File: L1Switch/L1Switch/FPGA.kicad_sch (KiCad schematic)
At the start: 9 parts, among them J11 Conn_01x06_Male, U1 XC7A35T-FTG256, X1 LFSPXO076034CUTT

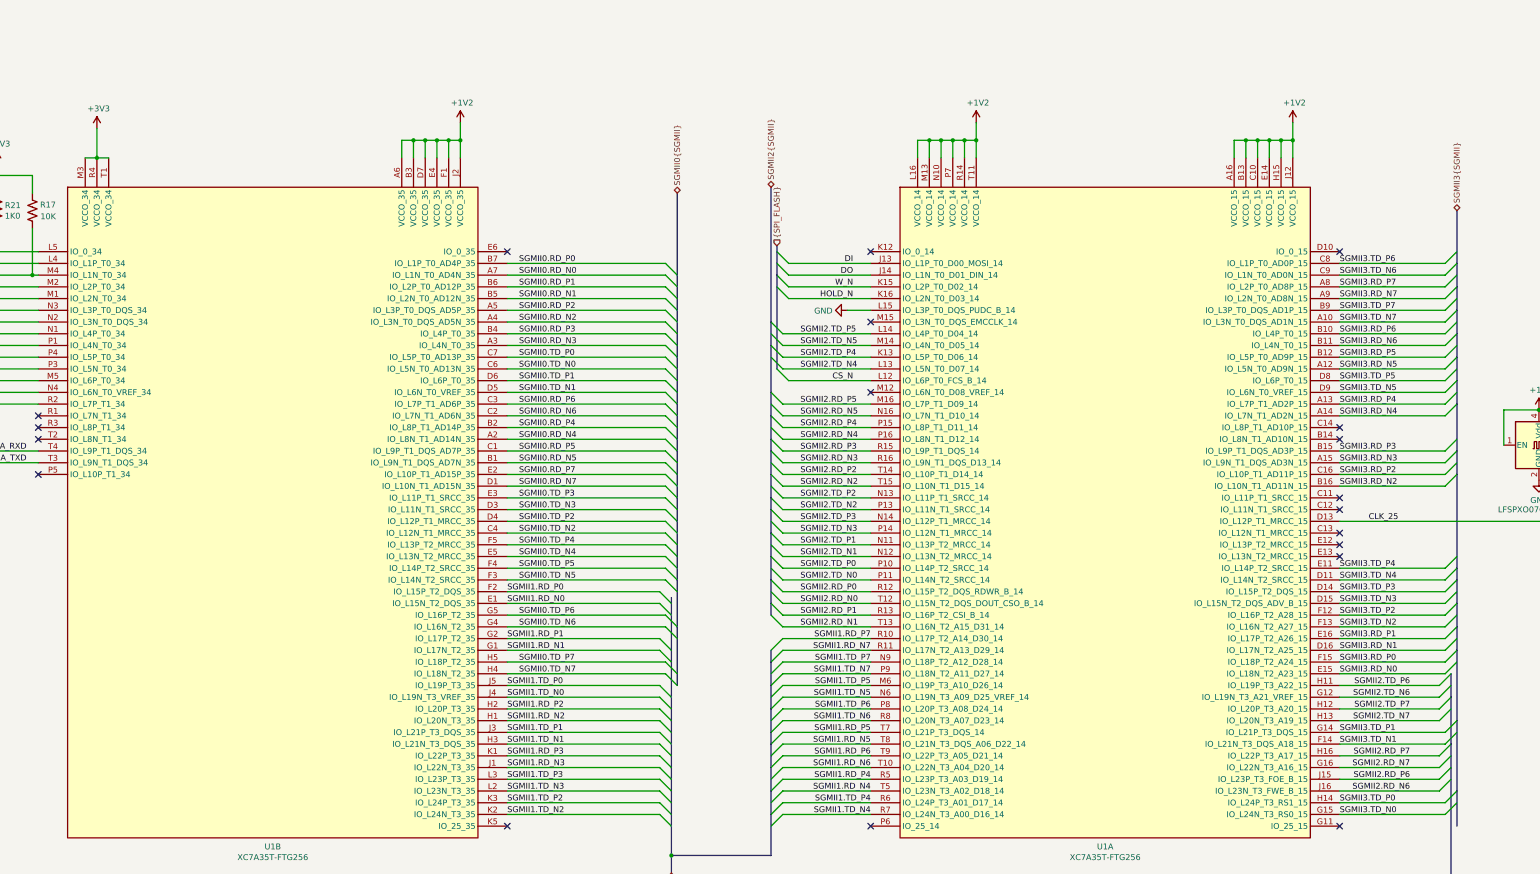
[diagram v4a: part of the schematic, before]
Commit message: Add FPGA decoupling caps. Add some power planes.
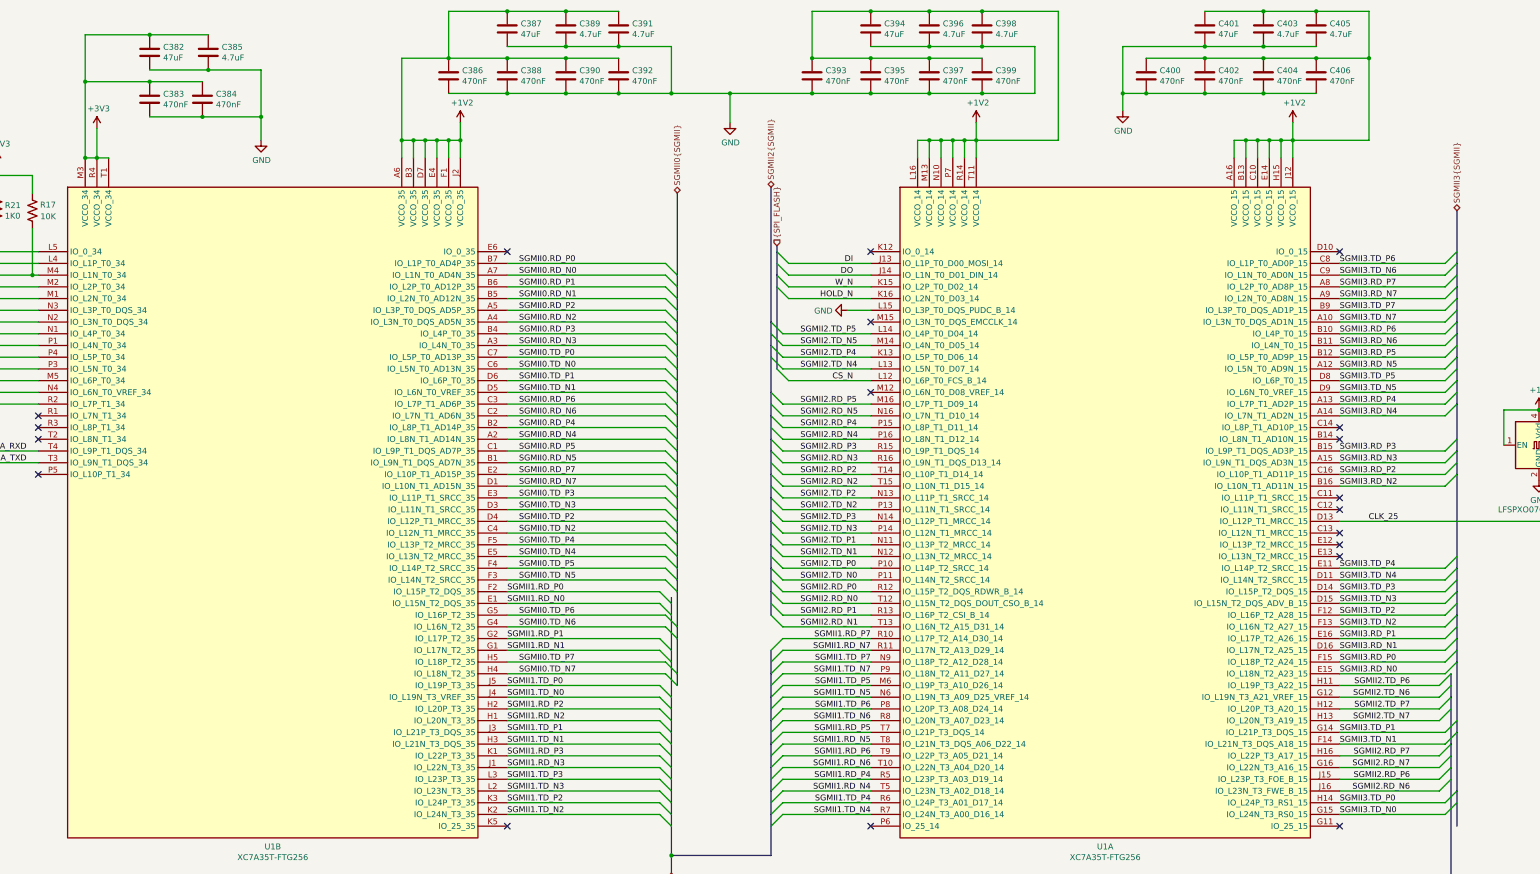
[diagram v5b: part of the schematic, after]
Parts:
- added C382, C387, C394, C401: 47uF, Capacitor_SMD:C_1210_3225Metric, symbol Device:C
- added C383, C384, C386, C388, C390, C392, C393, C395, C397, C399, C400, C402, C404, C406: 470nF, Capacitor_SMD:C_0402_1005Metric, symbol Device:C
- added C385, C389, C391, C396, C398, C403, C405: 4.7uF, Capacitor_SMD:C_0805_2012Metric, symbol Device:C
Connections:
- net +1V2: now also C386.1, C387.1, C388.1, C389.1, C390.1, C391.1, C392.1, C393.1, C394.1, C395.1, C396.1, C397.1, C398.1, C399.1, C400.1, C401.1, C402.1, C403.1, C404.1, C405.1, C406.1
- net +3V3: now also C382.1, C383.1, C384.1, C385.1
- net GND: now also C382.2, C383.2, C384.2, C385.2, C386.2, C387.2, C388.2, C389.2, C390.2, C391.2, C392.2, C393.2, C394.2, C395.2, C396.2, C397.2, C398.2, C399.2, C400.2, C401.2, C402.2, C403.2, C404.2, C405.2, C406.2

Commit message: Add some part info. Fix footprint size for 2kV caps. Add a plane cutout around the magnetics.
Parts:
- C382, C387, C394, C401: value 47uF -> 47 uF; MFR Part# (none) -> GRM32EB31A476KE20L; Manufacturer (none) -> MuRata
- C383, C384, C386, C388, C390, C392, C393, C395, C397, C399, C400, C402, C404, C406: value 470nF -> 470 nF; MFR Part# (none) -> GRM155R61C474KE01D; Manufacturer (none) -> MuRata
- C385, C389, C391, C396, C398, C403, C405: value 4.7uF -> 4.7 uF; MFR Part# (none) -> C0805C475K9PAC; Manufacturer (none) -> Kemet
- J11: MFR Part# (none) -> 68000-106HLF; Manufacturer (none) -> Amphenol
- U1: MFR Part# (none) -> XC7A35T-2FTG256C; Manufacturer (none) -> Xilinx
- X1: MFR Part# (none) -> LFSPXO076034CUTT; Manufacturer (none) -> IQD

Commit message: Update part numbers.
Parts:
- R135, R136, R137, R21: MFR Part# (none) -> CRCW04021K00FKEE; Manufacturer (none) -> Vishay
- R17: value 10K -> 10K0; MFR Part# (none) -> CRCW040210K0FKED; Manufacturer (none) -> Vishay
- TP1: MFR Part# (none) -> -; Manufacturer (none) -> -
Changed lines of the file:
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@@
 (kicad_sch (version 20200608) (host eeschema "5.99.0-unknown-1973153~101~ubuntu20.04.1")
-  (page 2 12)
+  (page 1 12)
   (paper "B")
   (bus_alias "MAC1_SGMII" (members ))
@@
   (junction (at 414.02 125.73))
   (junction (at 213.36 198.12))
+  (no_connect (at 358.14 107.95))
+  (no_connect (at 256.54 82.55))
   (no_connect (at 76.2 105.41))
-  (no_connect (at 358.14 105.41))
+  (no_connect (at 46.99 116.84))
+  (no_connect (at 177.8 67.31))
+  (no_connect (at 76.2 107.95))
+  (no_connect (at 358.14 120.65))
+  (no_connect (at 76.2 115.57))
+  (no_connect (at 358.14 133.35))
+  (no_connect (at 358.14 191.77))
+  (no_connect (at 256.54 67.31))
+  (no_connect (at 358.14 128.27))
+  (no_connect (at 358.14 130.81))
+  (no_connect (at 256.54 191.77))
+  (no_connect (at 46.99 114.3))
+  (no_connect (at 177.8 191.77))
   (no_connect (at 46.99 124.46))
-  (no_connect (at 177.8 191.77))
-  (no_connect (at 177.8 67.31))
-  (no_connect (at 76.2 102.87))
-  (no_connect (at 358.14 120.65))
-  (no_connect (at 358.14 128.27))
-  (no_connect (at 358.14 191.77))
-  (no_connect (at 358.14 130.81))
-  (no_connect (at 358.14 133.35))
-  (no_connect (at 76.2 107.95))
-  (no_connect (at 256.54 67.31))
-  (no_connect (at 256.54 191.77))
-  (no_connect (at 76.2 115.57))
-  (no_connect (at 256.54 82.55))
-  (no_connect (at 46.99 116.84))
   (no_connect (at 256.54 97.79))
   (no_connect (at 358.14 123.19))
   (no_connect (at 358.14 67.31))
-  (no_connect (at 358.14 107.95))
-  (no_connect (at 46.99 114.3))
+  (no_connect (at 358.14 105.41))
+  (no_connect (at 76.2 102.87))
   (bus_entry (at 210.82 140.97) (size 2.54 2.54))
   (bus_entry (at 210.82 143.51) (size 2.54 2.54))
@@
     (stroke (width 0) (type solid) (color 0 0 0 0))
   )
-  (bus (pts (xy 214.63 54.61) (xy 214.63 72.39))
-    (stroke (width 0) (type solid) (color 0 0 0 0))
-  )
-  (bus (pts (xy 214.63 72.39) (xy 214.63 77.47))
-    (stroke (width 0) (type solid) (color 0 0 0 0))
-  )
-  (bus (pts (xy 214.63 77.47) (xy 214.63 80.01))
-    (stroke (width 0) (type solid) (color 0 0 0 0))
-  )
-  (bus (pts (xy 214.63 80.01) (xy 214.63 85.09))
+  (bus (pts (xy 214.63 54.61) (xy 214.63 74.93))
+    (stroke (width 0) (type solid) (color 0 0 0 0))
+  )
+  (bus (pts (xy 214.63 74.93) (xy 214.63 77.47))
+    (stroke (width 0) (type solid) (color 0 0 0 0))
+  )
+  (bus (pts (xy 214.63 77.47) (xy 214.63 82.55))
+    (stroke (width 0) (type solid) (color 0 0 0 0))
+  )
+  (bus (pts (xy 214.63 82.55) (xy 214.63 85.09))
     (stroke (width 0) (type solid) (color 0 0 0 0))
   )
@@
     (stroke (width 0) (type solid) (color 0 0 0 0))
   )
-  (bus (pts (xy 214.63 90.17) (xy 214.63 92.71))
-    (stroke (width 0) (type solid) (color 0 0 0 0))
-  )
-  (bus (pts (xy 214.63 92.71) (xy 214.63 97.79))
-    (stroke (width 0) (type solid) (color 0 0 0 0))
-  )
-  (bus (pts (xy 214.63 97.79) (xy 214.63 102.87))
+  (bus (pts (xy 214.63 90.17) (xy 214.63 95.25))
+    (stroke (width 0) (type solid) (color 0 0 0 0))
+  )
+  (bus (pts (xy 214.63 95.25) (xy 214.63 100.33))
+    (stroke (width 0) (type solid) (color 0 0 0 0))
+  )
+  (bus (pts (xy 214.63 100.33) (xy 214.63 102.87))
     (stroke (width 0) (type solid) (color 0 0 0 0))
   )
@@
     (stroke (width 0) (type solid) (color 0 0 0 0))
   )
-  (bus (pts (xy 214.63 107.95) (xy 214.63 113.03))
-    (stroke (width 0) (type solid) (color 0 0 0 0))
-  )
-  (bus (pts (xy 214.63 113.03) (xy 214.63 118.11))
-    (stroke (width 0) (type solid) (color 0 0 0 0))
-  )
-  (bus (pts (xy 214.63 118.11) (xy 214.63 123.19))
+  (bus (pts (xy 214.63 107.95) (xy 214.63 110.49))
+    (stroke (width 0) (type solid) (color 0 0 0 0))
+  )
+  (bus (pts (xy 214.63 110.49) (xy 214.63 115.57))
+    (stroke (width 0) (type solid) (color 0 0 0 0))
+  )
+  (bus (pts (xy 214.63 115.57) (xy 214.63 120.65))
+    (stroke (width 0) (type solid) (color 0 0 0 0))
+  )
+  (bus (pts (xy 214.63 120.65) (xy 214.63 123.19))
     (stroke (width 0) (type solid) (color 0 0 0 0))
   )
@@
     (stroke (width 0) (type solid) (color 0 0 0 0))
   )
-  (bus (pts (xy 234.95 53.34) (xy 234.95 82.55))
-    (stroke (width 0) (type solid) (color 0 0 0 0))
-  )
-  (bus (pts (xy 234.95 82.55) (xy 234.95 87.63))
+  (bus (pts (xy 234.95 53.34) (xy 234.95 85.09))
+    (stroke (width 0) (type solid) (color 0 0 0 0))
+  )
+  (bus (pts (xy 234.95 85.09) (xy 234.95 87.63))
     (stroke (width 0) (type solid) (color 0 0 0 0))
   )
@@
     (stroke (width 0) (type solid) (color 0 0 0 0))
   )
-  (bus (pts (xy 234.95 128.27) (xy 234.95 133.35))
-    (stroke (width 0) (type solid) (color 0 0 0 0))
-  )
-  (bus (pts (xy 234.95 133.35) (xy 234.95 138.43))
-    (stroke (width 0) (type solid) (color 0 0 0 0))
-  )
-  (bus (pts (xy 234.95 138.43) (xy 234.95 140.97))
+  (bus (pts (xy 234.95 128.27) (xy 234.95 130.81))
+    (stroke (width 0) (type solid) (color 0 0 0 0))
+  )
+  (bus (pts (xy 234.95 130.81) (xy 234.95 135.89))
+    (stroke (width 0) (type solid) (color 0 0 0 0))
+  )
+  (bus (pts (xy 234.95 135.89) (xy 234.95 140.97))
     (stroke (width 0) (type solid) (color 0 0 0 0))
   )
@@
     (stroke (width 0) (type solid) (color 0 0 0 0))
   )
-  (bus (pts (xy 234.95 163.83) (xy 234.95 166.37))
-    (stroke (width 0) (type solid) (color 0 0 0 0))
-  )
-  (bus (pts (xy 234.95 166.37) (xy 234.95 171.45))
-    (stroke (width 0) (type solid) (color 0 0 0 0))
-  )
-  (bus (pts (xy 234.95 171.45) (xy 234.95 176.53))
-    (stroke (width 0) (type solid) (color 0 0 0 0))
-  )
-  (bus (pts (xy 234.95 176.53) (xy 234.95 181.61))
+  (bus (pts (xy 234.95 163.83) (xy 234.95 168.91))
+    (stroke (width 0) (type solid) (color 0 0 0 0))
+  )
+  (bus (pts (xy 234.95 168.91) (xy 234.95 173.99))
+    (stroke (width 0) (type solid) (color 0 0 0 0))
+  )
+  (bus (pts (xy 234.95 173.99) (xy 234.95 179.07))
+    (stroke (width 0) (type solid) (color 0 0 0 0))
+  )
+  (bus (pts (xy 234.95 179.07) (xy 234.95 181.61))
     (stroke (width 0) (type solid) (color 0 0 0 0))
   )
@@
     (stroke (width 0) (type solid) (color 0 0 0 0))
   )
-  (bus (pts (xy 236.22 69.85) (xy 236.22 72.39))
-    (stroke (width 0) (type solid) (color 0 0 0 0))
-  )
-  (bus (pts (xy 236.22 72.39) (xy 236.22 92.71))
+  (bus (pts (xy 236.22 69.85) (xy 236.22 74.93))
+    (stroke (width 0) (type solid) (color 0 0 0 0))
+  )
+  (bus (pts (xy 236.22 74.93) (xy 236.22 92.71))
     (stroke (width 0) (type solid) (color 0 0 0 0))
   )
@@
       (effects (font (size 1.27 1.27)) hide)
     )
+    (property "MFR Part#" "-" (id 4) (at 414.02 125.73 0)
+      (effects (font (size 1.27 1.27)) hide)
+    )
+    (property "Manufacturer" "-" (id 5) (at 414.02 125.73 0)
+      (effects (font (size 1.27 1.27)) hide)
+    )
   )
   (symbol (lib_id "power:+3V3") (at 67.31 48.26 0) (unit 1)
@@
       (effects (font (size 1.27 1.27)) hide)
     )
+    (property "MFR Part#" "CRCW04021K00FKEE" (id 4) (at 44.45 58.42 0)
+      (effects (font (size 1.27 1.27)) hide)
+    )
+    (property "Manufacturer" "Vishay" (id 5) (at 44.45 58.42 0)
+      (effects (font (size 1.27 1.27)) hide)
+    )
   )
   (symbol (lib_id "Device:R_US") (at 52.07 58.42 0) (unit 1)
@@
       (effects (font (size 1.27 1.27)) hide)
     )
+    (property "MFR Part#" "CRCW04021K00FKEE" (id 4) (at 52.07 58.42 0)
+      (effects (font (size 1.27 1.27)) hide)
+    )
+    (property "Manufacturer" "Vishay" (id 5) (at 52.07 58.42 0)
+      (effects (font (size 1.27 1.27)) hide)
+    )
   )
   (symbol (lib_id "Device:R_US") (at 59.69 58.42 0) (unit 1)
@@
       (effects (font (size 1.27 1.27)) hide)
     )
+    (property "MFR Part#" "CRCW04021K00FKEE" (id 4) (at 59.69 58.42 0)
+      (effects (font (size 1.27 1.27)) hide)
+    )
+    (property "Manufacturer" "Vishay" (id 5) (at 59.69 58.42 0)
+      (effects (font (size 1.27 1.27)) hide)
+    )
   )
   (symbol (lib_id "Device:R_US") (at 67.31 58.42 0) (unit 1)
@@
       (effects (font (size 1.27 1.27)) hide)
     )
+    (property "MFR Part#" "CRCW04021K00FKEE" (id 4) (at 67.31 58.42 0)
+      (effects (font (size 1.27 1.27)) hide)
+    )
+    (property "Manufacturer" "Vishay" (id 5) (at 67.31 58.42 0)
+      (effects (font (size 1.27 1.27)) hide)
+    )
   )
   (symbol (lib_id "Device:R_US") (at 74.93 58.42 180) (unit 1)
@@
       (effects (font (size 1.27 1.27)) (justify left))
     )
-    (property "Value" "10K" (id 1) (at 80.01 59.69 0)
+    (property "Value" "10K0" (id 1) (at 80.01 59.69 0)
       (effects (font (size 1.27 1.27)) (justify left))
     )
@@
       (effects (font (size 1.27 1.27)) hide)
     )
+    (property "MFR Part#" "CRCW040210K0FKED" (id 4) (at 74.93 58.42 0)
+      (effects (font (size 1.27 1.27)) hide)
+    )
+    (property "Manufacturer" "Vishay" (id 5) (at 74.93 58.42 0)
+      (effects (font (size 1.27 1.27)) hide)
+    )
